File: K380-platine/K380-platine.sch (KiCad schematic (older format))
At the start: 25 parts, among them J1 JST-PH 2, J2 Conn_01x23, J3 MicroMod-M.2E, J4 USB_C_Receptacle_USB2.0, Q1 PMost Enc FET -20V, Q2 Q_NMOS_DGS, U1 XC6220B331MR, U2 MCP73831-2-OT

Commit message: Add status LEDs
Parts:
- added D3, D4, D5, D6: WS2812B, LibraryLoader:WS28122020, symbol LED:WS2812B
- gave numbers to parts that had none: 5
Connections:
- net GND: now also D3.3 (VSS), D4.3 (VSS), D5.3 (VSS), D6.3 (VSS)
- net V3.3: now also D3.1 (VDD), D4.1 (VDD), D5.1 (VDD), D6.1 (VDD)
- new net: D5.2 (DOUT), D6.4 (DIN)
- new net: D4.2 (DOUT), D5.4 (DIN)
- new net: D3.2 (DOUT), D4.4 (DIN)
- new net DLED: D3.4 (DIN)
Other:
- note added: "Status LEDs"
- moved on the sheet: J2, SW2, SW3
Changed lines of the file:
@@
 L Connector_Generic:Conn_01x23 J2
 U 1 1 62906B4C
-P 7650 6100
-F 0 "J2" V 7775 6096 50  0000 C CNN
-F 1 "Conn_01x23" V 7866 6096 50  0000 C CNN
-F 2 "Connector_FFC-FPC:TE_2-84952-3_1x23-1MP_P1.0mm_Horizontal" H 7650 6100 50  0001 C CNN
-F 3 "~" H 7650 6100 50  0001 C CNN
-	1    7650 6100
+P 6800 2050
+F 0 "J2" V 6925 2046 50  0000 C CNN
+F 1 "Conn_01x23" V 7016 2046 50  0000 C CNN
+F 2 "Connector_FFC-FPC:TE_2-84952-3_1x23-1MP_P1.0mm_Horizontal" H 6800 2050 50  0001 C CNN
+F 3 "~" H 6800 2050 50  0001 C CNN
+	1    6800 2050
 	0    1    1    0
 $EndComp
@@
 	1650 8900 1650 8850
 $Comp
-L power:GND #PWR?
+L power:GND #PWR07
 U 1 1 629C1EB6
 P 12050 9950
-F 0 "#PWR?" H 12050 9700 50  0001 C CNN
+F 0 "#PWR07" H 12050 9700 50  0001 C CNN
 F 1 "GND" H 12055 9777 50  0000 C CNN
 F 2 "" H 12050 9950 50  0001 C CNN
@@
 VBAT
 $Comp
-L Device:R_Small R?
+L Device:R_Small R8
 U 1 1 629C2DD2
 P 12050 9400
-F 0 "R?" H 12109 9446 50  0000 L CNN
+F 0 "R8" H 12109 9446 50  0000 L CNN
 F 1 "100K" H 12109 9355 50  0000 L CNN
 F 2 "" H 12050 9400 50  0001 C CNN
@@
 $EndComp
 $Comp
-L Device:R_Small R?
+L Device:R_Small R9
 U 1 1 629C30FE
 P 12050 9800
-F 0 "R?" H 12109 9846 50  0000 L CNN
+F 0 "R9" H 12109 9846 50  0000 L CNN
 F 1 "100K" H 12109 9755 50  0000 L CNN
 F 2 "" H 12050 9800 50  0001 C CNN
@@
 	13000 7950 13000 11200
 $Comp
-L Switch:SW_DPST_x2 SW?
+L Switch:SW_DPST_x2 SW1
 U 1 1 629D6AE3
 P 2150 8900
-F 0 "SW?" H 2150 9135 50  0000 C CNN
+F 0 "SW1" H 2150 9135 50  0000 C CNN
 F 1 "EG1215AA" H 2150 9044 50  0000 C CNN
 F 2 "LibraryLoader:EG1215AA" H 2150 8900 50  0001 C CNN
@@
 	2500 8900 2350 8900
 $Comp
-L power:GND #PWR?
+L power:GND #PWR09
 U 1 1 629DCBD7
-P 14000 9100
-F 0 "#PWR?" H 14000 8850 50  0001 C CNN
-F 1 "GND" H 14005 8927 50  0000 C CNN
-F 2 "" H 14000 9100 50  0001 C CNN
-F 3 "" H 14000 9100 50  0001 C CNN
-	1    14000 9100
-	1    0    0    -1
-$EndComp
-$Comp
-L Switch:SW_Push SW?
+P 14000 9300
+F 0 "#PWR09" H 14000 9050 50  0001 C CNN
+F 1 "GND" H 14005 9127 50  0000 C CNN
+F 2 "" H 14000 9300 50  0001 C CNN
+F 3 "" H 14000 9300 50  0001 C CNN
+	1    14000 9300
+	1    0    0    -1
+$EndComp
+$Comp
+L Switch:SW_Push SW2
 U 1 1 629DE056
-P 14300 9000
-F 0 "SW?" H 14300 9285 50  0000 C CNN
-F 1 "SW_Push" H 14300 9194 50  0000 C CNN
-F 2 "" H 14300 9200 50  0001 C CNN
-F 3 "~" H 14300 9200 50  0001 C CNN
-	1    14300 9000
-	1    0    0    -1
-$EndComp
-Wire Wire Line
-	14000 9000 14100 9000
-Text GLabel 14700 9000 2    79   Input ~ 0
+P 14300 9200
+F 0 "SW2" H 14300 9485 50  0000 C CNN
+F 1 "SW_Push" H 14300 9394 50  0000 C CNN
+F 2 "" H 14300 9400 50  0001 C CNN
+F 3 "~" H 14300 9400 50  0001 C CNN
+	1    14300 9200
+	1    0    0    -1
+$EndComp
+Wire Wire Line
+	14000 9200 14100 9200
+Text GLabel 14700 9200 2    79   Input ~ 0
 RESET
 $Comp
-L power:GND #PWR?
+L power:GND #PWR010
 U 1 1 629E30F9
-P 14000 9950
-F 0 "#PWR?" H 14000 9700 50  0001 C CNN
-F 1 "GND" H 14005 9777 50  0000 C CNN
-F 2 "" H 14000 9950 50  0001 C CNN
-F 3 "" H 14000 9950 50  0001 C CNN
-	1    14000 9950
-	1    0    0    -1
-$EndComp
-$Comp
-L Switch:SW_Push SW?
+P 14000 10150
+F 0 "#PWR010" H 14000 9900 50  0001 C CNN
+F 1 "GND" H 14005 9977 50  0000 C CNN
+F 2 "" H 14000 10150 50  0001 C CNN
+F 3 "" H 14000 10150 50  0001 C CNN
+	1    14000 10150
+	1    0    0    -1
+$EndComp
+$Comp
+L Switch:SW_Push SW3
 U 1 1 629E3139
-P 14300 9850
-F 0 "SW?" H 14300 10135 50  0000 C CNN
-F 1 "SW_Push" H 14300 10044 50  0000 C CNN
-F 2 "" H 14300 10050 50  0001 C CNN
-F 3 "~" H 14300 10050 50  0001 C CNN
-	1    14300 9850
-	1    0    0    -1
-$EndComp
-Text GLabel 14700 9850 2    79   Input ~ 0
+P 14300 10050
+F 0 "SW3" H 14300 10335 50  0000 C CNN
+F 1 "SW_Push" H 14300 10244 50  0000 C CNN
+F 2 "" H 14300 10250 50  0001 C CNN
+F 3 "~" H 14300 10250 50  0001 C CNN
+	1    14300 10050
+	1    0    0    -1
+$EndComp
+Text GLabel 14700 10050 2    79   Input ~ 0
 SWITCH
 Wire Wire Line
-	14000 9950 14000 9850
-Wire Wire Line
-	14000 9850 14100 9850
-Wire Wire Line
-	14500 9850 14700 9850
-Wire Wire Line
-	14700 9000 14500 9000
-Wire Wire Line
-	14000 9100 14000 9000
+	14000 10150 14000 10050
+Wire Wire Line
+	14000 10050 14100 10050
+Wire Wire Line
+	14500 10050 14700 10050
+Wire Wire Line
+	14700 9200 14500 9200
+Wire Wire Line
+	14000 9300 14000 9200
 Text Notes 13950 8300 0    79   ~ 0
 Reset/User Switch
 Wire Notes Line
 	500  7950 16050 7950
+$Comp
+L LED:WS2812B D4
+U 1 1 629F6F87
+P 13900 6250
+F 0 "D4" H 14244 6296 50  0000 L CNN
+F 1 "WS2812B" H 14244 6205 50  0000 L CNN
+F 2 "LibraryLoader:WS28122020" H 13950 5950 50  0001 L TNN
+F 3 "https://cdn-shop.adafruit.com/datasheets/WS2812B.pdf" H 14000 5875 50  0001 L TNN
+	1    13900 6250
+	1    0    0    -1
+$EndComp
+$Comp
+L LED:WS2812B D6
+U 1 1 629F5E89
+P 14750 7200
+F 0 "D6" H 14406 7154 50  0000 R CNN
+F 1 "WS2812B" H 14406 7245 50  0000 R CNN
+F 2 "LibraryLoader:WS28122020" H 14800 6900 50  0001 L TNN
+F 3 "https://cdn-shop.adafruit.com/datasheets/WS2812B.pdf" H 14850 6825 50  0001 L TNN
+	1    14750 7200
+	-1   0    0    1
+$EndComp
+$Comp
+L LED:WS2812B D5
+U 1 1 629F6B68
+P 14750 6250
+F 0 "D5" H 15094 6296 50  0000 L CNN
+F 1 "WS2812B" H 15094 6205 50  0000 L CNN
+F 2 "LibraryLoader:WS28122020" H 14800 5950 50  0001 L TNN
+F 3 "https://cdn-shop.adafruit.com/datasheets/WS2812B.pdf" H 14850 5875 50  0001 L TNN
+	1    14750 6250
+	1    0    0    -1
+$EndComp
+$Comp
+L LED:WS2812B D3
+U 1 1 629FDF90
+P 13000 6250
+F 0 "D3" H 13344 6296 50  0000 L CNN
+F 1 "WS2812B" H 13344 6205 50  0000 L CNN
+F 2 "LibraryLoader:WS28122020" H 13050 5950 50  0001 L TNN
+F 3 "https://cdn-shop.adafruit.com/datasheets/WS2812B.pdf" H 13100 5875 50  0001 L TNN
+	1    13000 6250
+	1    0    0    -1
+$EndComp
+Text GLabel 12400 6250 0    79   Input ~ 0
+DLED
+Wire Wire Line
+	12400 6250 12700 6250
+Wire Wire Line
+	13300 6250 13600 6250
+Wire Wire Line
+	14200 6250 14450 6250
+Wire Wire Line
+	15050 7200 15200 7200
+Wire Wire Line
+	15200 7200 15200 6250
+Wire Wire Line
+	15200 6250 15050 6250
+$Comp
+L power:GND #PWR08
+U 1 1 62A113D2
+P 13000 6900
+F 0 "#PWR08" H 13000 6650 50  0001 C CNN
+F 1 "GND" H 13005 6727 50  0000 C CNN
+F 2 "" H 13000 6900 50  0001 C CNN
+F 3 "" H 13000 6900 50  0001 C CNN
+	1    13000 6900
+	1    0    0    -1
+$EndComp
+Text GLabel 13000 5650 1    79   Output ~ 0
+V3.3
+Wire Wire Line
+	13000 6900 13000 6600
+Wire Wire Line
+	13000 6600 13900 6600
+Wire Wire Line
+	14750 6600 14750 6900
+Connection ~ 13000 6600
+Wire Wire Line
+	13000 6600 13000 6550
+Wire Wire Line
+	14750 6600 14750 6550
+Connection ~ 14750 6600
+Wire Wire Line
+	13900 6600 13900 6550
+Connection ~ 13900 6600
+Wire Wire Line
+	13900 6600 14750 6600
+Wire Wire Line
+	13000 5950 13000 5900
+Wire Wire Line
+	13000 5900 13900 5900
+Wire Wire Line
+	15600 5900 15600 7550
+Wire Wire Line
+	15600 7550 14750 7550
+Wire Wire Line
+	14750 7550 14750 7500
+Connection ~ 13000 5900
+Wire Wire Line
+	13000 5900 13000 5650
+Wire Wire Line
+	13900 5950 13900 5900
+Connection ~ 13900 5900
+Wire Wire Line
+	13900 5900 14750 5900
+Wire Wire Line
+	14750 5950 14750 5900
+Connection ~ 14750 5900
+Wire Wire Line
+	14750 5900 15600 5900
+Text Notes 13500 4900 0    79   ~ 0
+Status LEDs
+Wire Notes Line
+	11600 7950 11600 4550
+Wire Notes Line
+	11600 4550 16050 4550
 $EndSCHEMATC

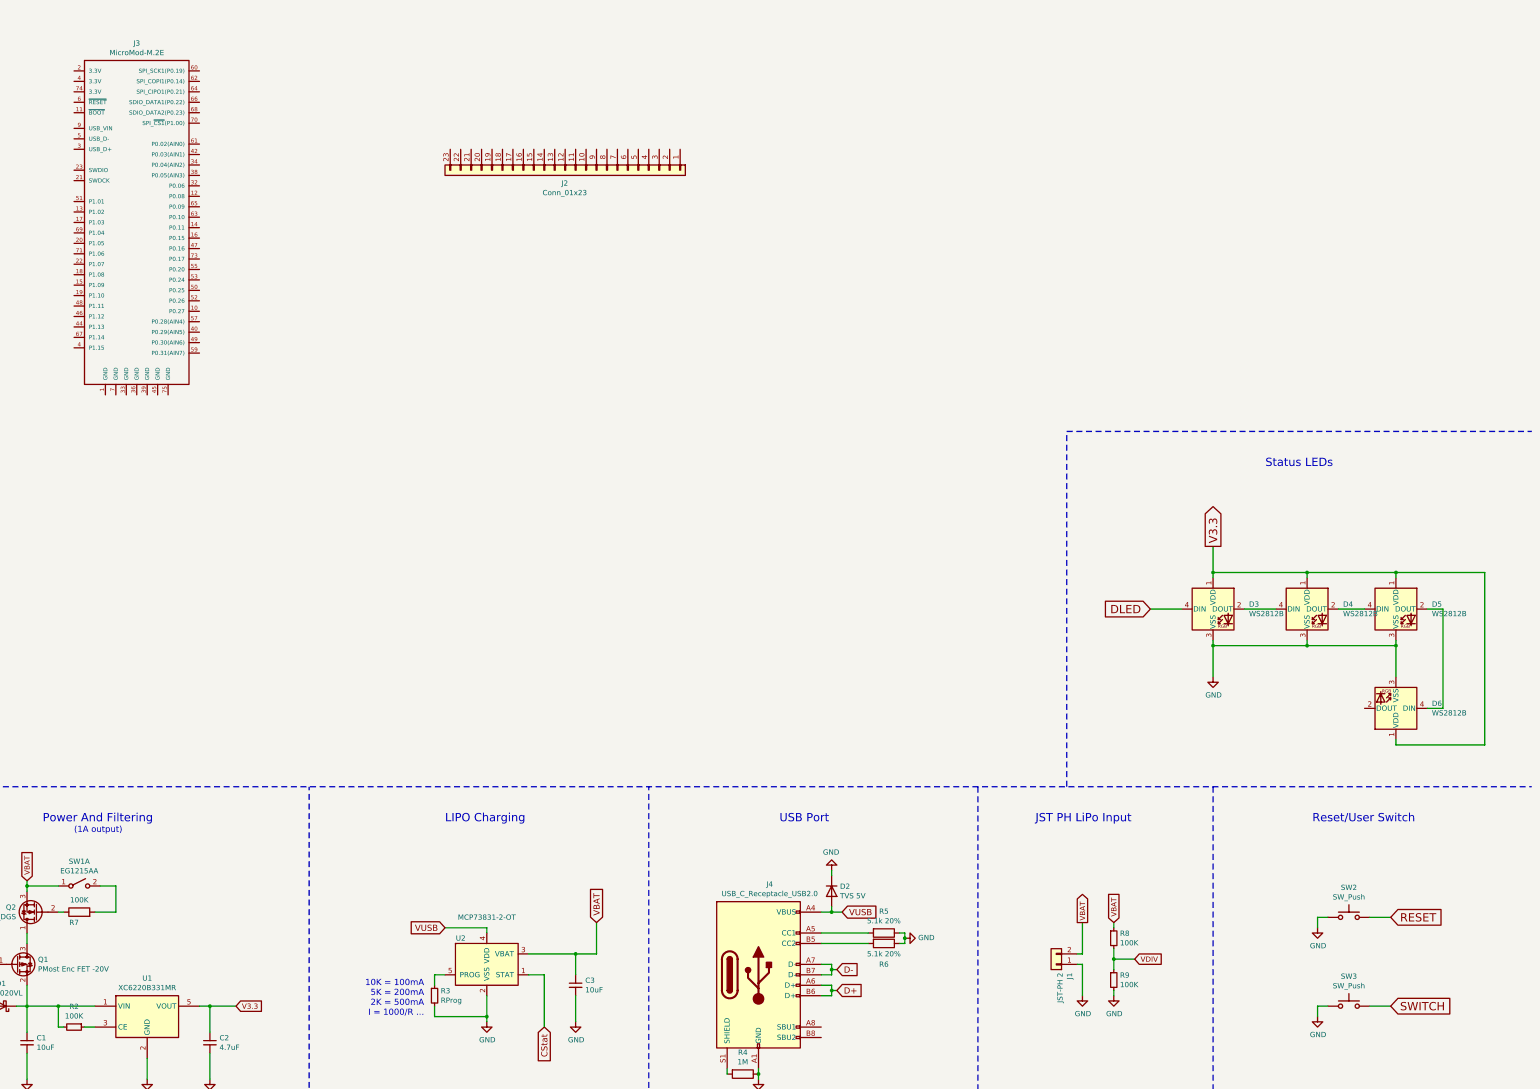
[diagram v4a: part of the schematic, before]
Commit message: Finish schematics
- decoupling capacitors
- connected keyboard matrix
- changed from user to boot pin
- add SWD connector
- connect MicroMod connector
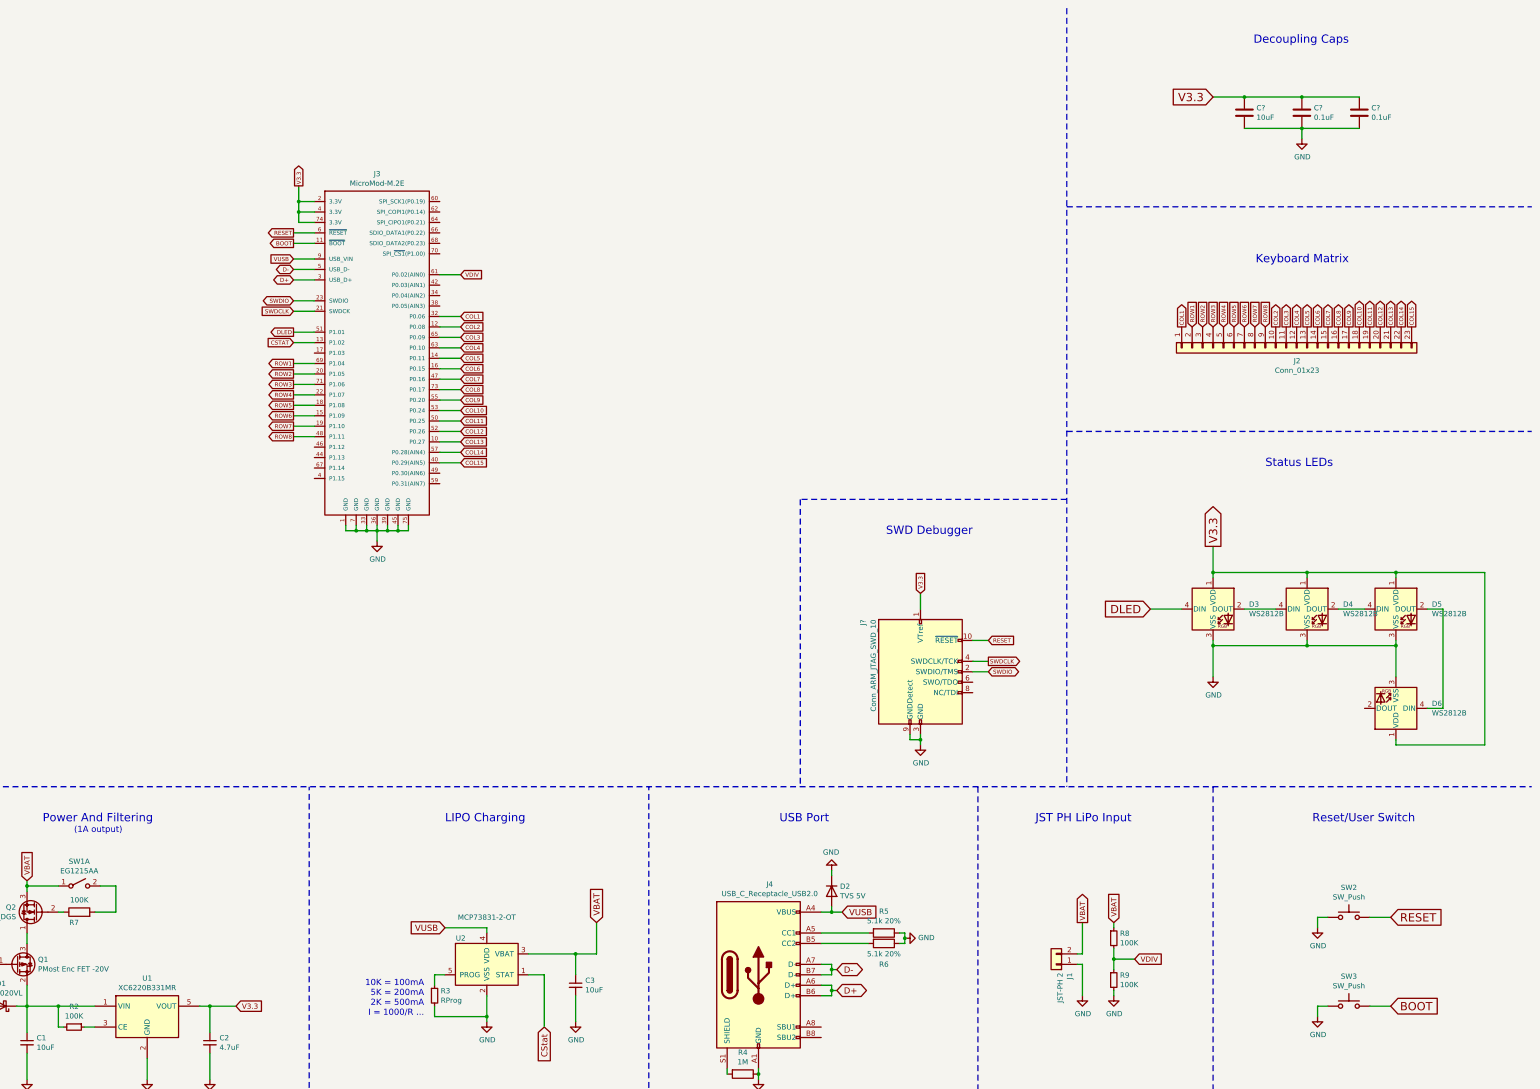
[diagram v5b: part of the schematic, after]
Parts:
- added C?: 10uF, symbol Device:C
- added C? (x2): 0.1uF, symbol Device:C
- added J?: Conn_ARM_JTAG_SWD_10, symbol Connector:Conn_ARM_JTAG_SWD_10
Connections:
- net SWITCH is gone; now on net BOOT: SW3.2
- net D+: now also J3.3 (USB_D+)
- net D-: now also J3.5 (USB_D-)
- net DLED: now also J3.51 (P1.01)
- net GND: now also J3.1 (GND), J3.33 (GND), J3.36 (GND), J3.39 (GND), J3.45 (GND), J3.7 (GND), J3.75 (GND), C?.2, C?.2, C?.2, J?.3 (GND), J?.5 (GND), J?.9 (GNDDetect)
- net RESET: now also J3.6 (~RESET), J?.10 (~RESET~)
- net V3.3: now also J3.2 (3.3V), J3.4 (P1.15), J3.74 (3.3V), C?.1, C?.1, C?.1, J?.1 (VTref)
- net VDIV: now also J3.61 (P0.02(AIN0))
- net VUSB: now also J3.9 (USB_VIN)
- net COL1: now reaches J2.1 (Pin_1)
- net COL1: now also J3.32 (P0.06)
- net COL2: now reaches J2.10 (Pin_10)
- net COL2: now also J3.12 (P0.08)
- net COL3: now reaches J2.11 (Pin_11)
- net COL3: now also J3.65 (P0.09)
- net COL4: now reaches J2.12 (Pin_12)
- net COL4: now also J3.63 (P0.10)
- net COL5: now reaches J2.13 (Pin_13)
- net COL5: now also J3.14 (P0.11)
- net COL6: now reaches J2.14 (Pin_14)
- net COL6: now also J3.16 (P0.15)
- net COL7: now reaches J2.15 (Pin_15)
- net COL7: now also J3.47 (P0.16)
- net COL8: now reaches J2.16 (Pin_16)
- net COL8: now also J3.73 (P0.17)
- net COL9: now reaches J2.17 (Pin_17)
- net COL9: now also J3.55 (P0.20)
- net COL10: now reaches J2.18 (Pin_18)
- net COL10: now also J3.53 (P0.24)
- net COL11: now reaches J2.19 (Pin_19)
- net COL11: now also J3.50 (P0.25)
- net ROW1: now reaches J2.2 (Pin_2)
- net ROW1: now also J3.69 (P1.04)
- net COL12: now reaches J2.20 (Pin_20)
- net COL12: now also J3.52 (P0.26)
- net COL13: now reaches J2.21 (Pin_21)
- net COL13: now also J3.10 (P0.27)
- net COL14: now reaches J2.22 (Pin_22)
- net COL14: now also J3.57 (P0.28(AIN4))
- net COL15: now reaches J2.23 (Pin_23)
- net COL15: now also J3.40 (P0.29(AIN5))
- net ROW2: now reaches J2.3 (Pin_3)
- net ROW2: now also J3.20 (P1.05)
- net ROW3: now reaches J2.4 (Pin_4)
- net ROW3: now also J3.71 (P1.06)
- net ROW4: now reaches J2.5 (Pin_5)
- net ROW4: now also J3.22 (P1.07)
- net ROW5: now reaches J2.6 (Pin_6)
- net ROW5: now also J3.18 (P1.08)
- net ROW6: now reaches J2.7 (Pin_7)
- net ROW6: now also J3.15 (P1.09)
- net ROW7: now reaches J2.8 (Pin_8)
- net ROW7: now also J3.19 (P1.10)
- net ROW8: now reaches J2.9 (Pin_9)
- net ROW8: now also J3.48 (P1.11)
- net BOOT: now reaches J3.11 (~BOOT)
- net CSTAT: now reaches J3.13 (P1.02)
- net SWDCLK: now reaches J3.21 (SWDCK)
- net SWDCLK: now also J?.4 (SWDCLK/TCK)
- net SWDIO: now reaches J3.23 (SWDIO)
- net SWDIO: now also J?.2 (SWDIO/TMS)
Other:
- note added: "Decoupling Caps"
- note added: "Keyboard Matrix"
- note added: "SWD Debugger"
- moved on the sheet: J2, J3
